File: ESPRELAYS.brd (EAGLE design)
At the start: 47 x 78 mm, 67 parts, among them IC1 ESP12SMT, J1 2.1MM DC Jack, K1 REED, K2 REED, K3 REED, K4 REED, K5 REED, K6 REED, Q1 2N7002, Q2 2N7002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

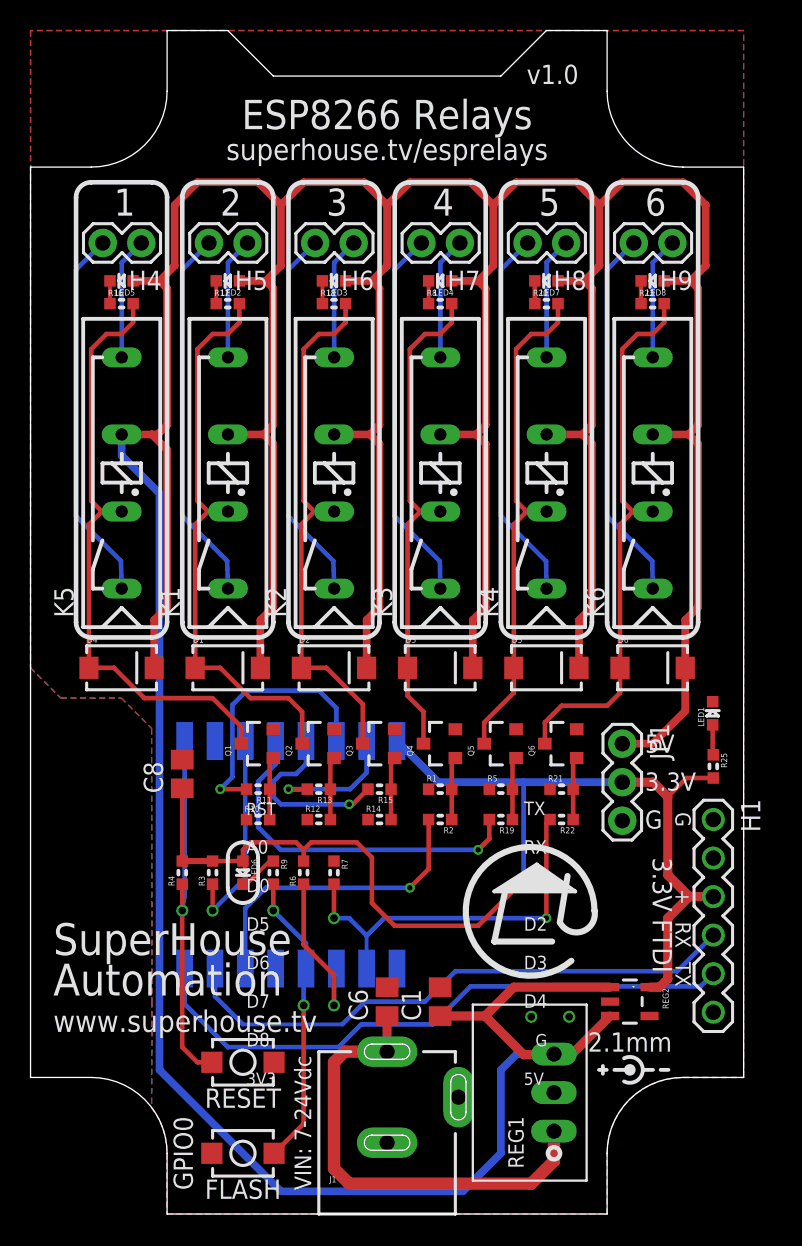
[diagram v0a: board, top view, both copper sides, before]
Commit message: Changed output pins to avoid GPIO16 because it pulses on startup. v1.1 release
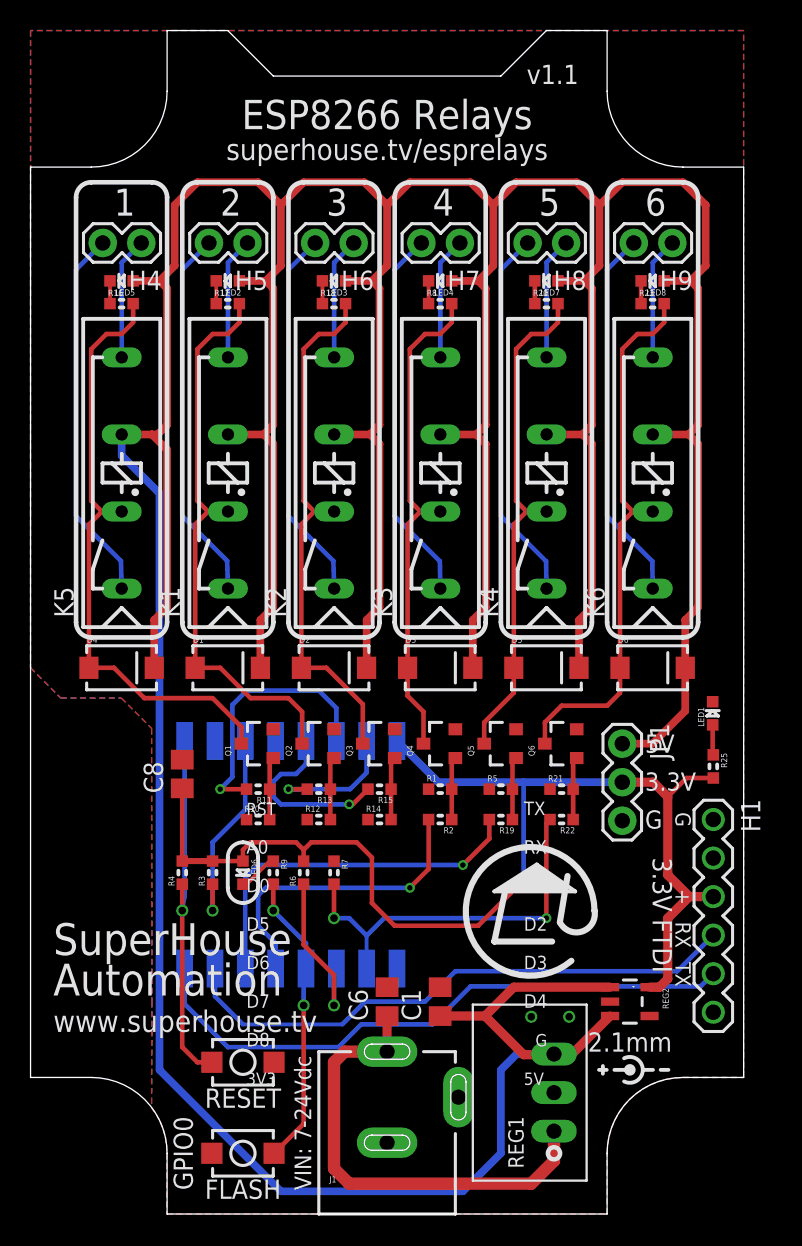
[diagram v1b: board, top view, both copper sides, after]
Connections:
- net GPIO16: no longer R19.2
- net GPIO4: now also R2.2
- net GPIO5: now also R19.2; no longer R2.2
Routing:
- net GPIO16: track 23.6 -> 0.00 mm, vias 1 -> 0
- net GPIO4: track 0.00 -> 20.5 mm, vias 0 -> 1
- net GPIO5: track 20.4 -> 24.4 mm
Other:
- board text added: "Output 1: GPIO12 Output 2: GPIO13 Output 3: GPIO14 Output 4: GPIO4 Output 5: GPIO5 Output 6: GPIO15"
- board text added: "v1.1"
- board text removed: "Output 1: GPIO12 Output 2: GPIO13 Output 3: GPIO14 Output 4: GPIO5 Output 5: GPIO16 Output 6: GPIO15"
- board text removed: "v1.0"
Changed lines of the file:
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@@
 <layer number="14" name="Route14" color="1" fill="6" visible="no" active="no"/>
 <layer number="15" name="Route15" color="4" fill="6" visible="no" active="no"/>
-<layer number="16" name="Bottom" color="1" fill="1" visible="no" active="yes"/>
+<layer number="16" name="Bottom" color="1" fill="1" visible="yes" active="yes"/>
 <layer number="17" name="Pads" color="2" fill="1" visible="yes" active="yes"/>
 <layer number="18" name="Vias" color="2" fill="1" visible="yes" active="yes"/>
 <layer number="19" name="Unrouted" color="12" fill="1" visible="yes" active="yes"/>
 <layer number="20" name="Dimension" color="15" fill="1" visible="yes" active="yes"/>
-<layer number="21" name="tPlace" color="15" fill="1" visible="no" active="yes"/>
-<layer number="22" name="bPlace" color="14" fill="1" visible="no" active="yes"/>
+<layer number="21" name="tPlace" color="15" fill="1" visible="yes" active="yes"/>
+<layer number="22" name="bPlace" color="14" fill="1" visible="yes" active="yes"/>
 <layer number="23" name="tOrigins" color="15" fill="1" visible="yes" active="yes"/>
 <layer number="24" name="bOrigins" color="3" fill="1" visible="yes" active="yes"/>
 <layer number="25" name="tNames" color="7" fill="1" visible="no" active="yes"/>
 <layer number="26" name="bNames" color="3" fill="1" visible="no" active="yes"/>
-<layer number="27" name="tValues" color="7" fill="1" visible="yes" active="yes"/>
+<layer number="27" name="tValues" color="7" fill="1" visible="no" active="yes"/>
 <layer number="28" name="bValues" color="3" fill="1" visible="no" active="yes"/>
 <layer number="29" name="tStop" color="7" fill="3" visible="no" active="yes"/>
@@
 <wire x1="32.854" y1="22.022" x2="33.362" y2="22.276" width="0.4064" layer="21"/>
 <text x="23.5" y="69.4632" size="1.4" layer="21" font="vector" ratio="15" rot="SR0" align="bottom-center">superhouse.tv/esprelays</text>
-<text x="32.698" y="74.476" size="1.27" layer="21" font="vector" ratio="18">v1.0</text>
+<text x="32.698" y="74.476" size="1.27" layer="21" font="vector" ratio="18">v1.1</text>
 <text x="31.16" y="72.476" size="1.27" layer="22" font="vector" ratio="18" rot="MR0">SKU: ESPRELAYS</text>
 <text x="18.5" y="6" size="1.1" layer="21" font="vector" ratio="18" rot="SR90" align="bottom-center">VIN: 7-24Vdc</text>
@@
 Output 2: GPIO13
 Output 3: GPIO14
-Output 4: GPIO5
-Output 5: GPIO16
+Output 4: GPIO4
+Output 5: GPIO5
 Output 6: GPIO15</text>
 <wire x1="39.119" y1="10.262" x2="39.119" y2="8.738" width="0.254" layer="21" curve="-233.130102"/>
@@
 <signal name="GPIO5">
 <contactref element="IC1" pad="14"/>
+<wire x1="14.154" y1="22.154" x2="14.154" y2="16.178" width="0.3048" layer="16"/>
+<wire x1="14.154" y1="22.154" x2="15" y2="23" width="0.3048" layer="16"/>
+<via x="28.5" y="23" extent="1-16" drill="0.3556"/>
+<wire x1="28.5" y1="23" x2="15" y2="23" width="0.3048" layer="16"/>
+<wire x1="28.5" y1="23" x2="30.238" y2="24.738" width="0.3048" layer="1"/>
+<contactref element="R19" pad="2"/>
+<wire x1="30.238" y1="24.738" x2="30.238" y2="26" width="0.3048" layer="1"/>
+</signal>
+<signal name="GPIO4">
+<contactref element="IC1" pad="13"/>
 <contactref element="R2" pad="2"/>
-<wire x1="14.154" y1="20.154" x2="14.154" y2="16.178" width="0.3048" layer="16"/>
-<wire x1="14.154" y1="20.154" x2="15.5" y2="21.5" width="0.3048" layer="16"/>
+<wire x1="16.154" y1="16.178" x2="16.154" y2="17.846" width="0.3048" layer="16"/>
+<wire x1="15" y1="19" x2="15" y2="21" width="0.3048" layer="16"/>
+<wire x1="15" y1="21" x2="15.5" y2="21.5" width="0.3048" layer="16"/>
+<wire x1="15.5" y1="21.5" x2="25" y2="21.5" width="0.3048" layer="16"/>
 <via x="25" y="21.5" extent="1-16" drill="0.3556"/>
-<wire x1="15.5" y1="21.5" x2="25" y2="21.5" width="0.3048" layer="16"/>
 <wire x1="25" y1="21.5" x2="26.238" y2="22.738" width="0.3048" layer="1"/>
 <wire x1="26.238" y1="22.738" x2="26.238" y2="26" width="0.3048" layer="1"/>
-</signal>
-<signal name="GPIO4">
-<contactref element="IC1" pad="13"/>
+<wire x1="16.154" y1="17.846" x2="15" y2="19" width="0.3048" layer="16"/>
 </signal>
 <signal name="GPIO14">
@@
 <signal name="GPIO16">
 <contactref element="IC1" pad="4"/>
-<contactref element="R19" pad="2"/>
-<wire x1="30.238" y1="26" x2="30.238" y2="24.738" width="0.3048" layer="1"/>
-<wire x1="30.238" y1="24.738" x2="29.5" y2="24" width="0.3048" layer="1"/>
-<via x="29.5" y="24" extent="1-16" drill="0.3556"/>
-<wire x1="16.5" y1="24" x2="15" y2="25.5" width="0.3048" layer="16"/>
-<wire x1="15" y1="25.5" x2="15" y2="28.5" width="0.3048" layer="16"/>
-<wire x1="16.154" y1="29.654" x2="16.154" y2="31.178" width="0.3048" layer="16"/>
-<wire x1="29.5" y1="24" x2="16.5" y2="24" width="0.3048" layer="16"/>
-<wire x1="15" y1="28.5" x2="16.154" y2="29.654" width="0.3048" layer="16"/>
 </signal>
 <signal name="GPIO0">
@@
 <wire x1="12" y1="21.738" x2="12" y2="20" width="0.3048" layer="1"/>
 <via x="12" y="20" extent="1-16" drill="0.5"/>
-<wire x1="12" y1="20" x2="14.154" y2="22.154" width="0.3048" layer="16"/>
-<wire x1="14.154" y1="22.154" x2="14.154" y2="31.178" width="0.3048" layer="16"/>
+<wire x1="14.154" y1="26.654" x2="12" y2="24.5" width="0.3048" layer="16"/>
+<wire x1="12" y1="20" x2="12" y2="24.5" width="0.3048" layer="16"/>
+<wire x1="14.154" y1="26.654" x2="14.154" y2="31.178" width="0.3048" layer="16"/>
 </signal>
 <signal name="ADC">

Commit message: Replaced most parts using SuperHouse library to add 3D models
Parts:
- removed H1: USB-TTL, freetronics:1X06
- added J2: Program, SuperHouse-Connectors:1X06-S
- C1, C6, C8: device freetronics-jon:C0805 -> SuperHouse-DiscreteSemi:C0805
- D1, D2, D3, D4, D5, D6: device SparkFun:SMA-DIODE -> SuperHouse-DiscreteSemi:SMA-DIODE
- H4, H5, H6, H7, H8, H9: device freetronics-jon:1X02 -> SuperHouse-Connectors:1X02-P
- IC1: value ESP12SMT -> ESP12-SMT; device freetronics-jon:ESP12 -> SuperHouse-MCUs:ESP12
- J1: device freetronics-jon:POWER_JACK_PTH_SLOTS -> SuperHouse-Connectors:POWER_JACK_SLOTS
- JP1: device freetronics-jon:1X03 -> SuperHouse-Connectors:1X03
- K1, K2, K3, K4, K5, K6: value REED -> REED-SIL; device relay:REED -> SuperHouse-Relays:REED
- LED1: device freetronics-jon:LED-0603 -> SuperHouse-LEDs:LED-0603
- LED2, LED3, LED4, LED5, LED6, LED7, LED8: device freetronics-master-v1:LED-0603 -> SuperHouse-LEDs:LED-0603
- Q1, Q2, Q3, Q4, Q5, Q6: device freetronics-master-v1:SOT23-3 -> SuperHouse-DiscreteSemi:SOT23-3
- R1, R10, R11, R12, R13, R14, R15, R16, R17, R18, R19, R2, R20, R21, R22, R23, R5, R8, R9: device freetronics-master-v1:0603 -> SuperHouse-DiscreteSemi:R0603
- R25, R3, R4, R6, R7: device freetronics-jon:0603 -> SuperHouse-DiscreteSemi:R0603
- REG1: device freetronics-jon:K78XX-500R3 -> SuperHouse-Regulators:K78XX-500R3
- REG2: device freetronics-jon:SOT23-5 -> SuperHouse-Regulators:SOT23-5
- S1, S2: device freetronics-jon:TACTILE_SWITCH_SMD_2PIN_TINY -> SuperHouse-Switches:TACTILE_SMD_3X4X2
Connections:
- net 3.3V: now also J2.6; no longer H1.3
- net GND: now also J2.3; no longer H1.1
- net GPIO0: now also J2.1
- net RST: now also J2.2
- net RX: now also J2.5; no longer H1.4
- net TX: now also J2.4; no longer H1.5
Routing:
- net RST: track 24.3 -> 73.6 mm, vias 1 -> 3
- net GPIO0: track 19.5 -> 50.9 mm
- net 3.3V: track 80.2 -> 81.4 mm
- net TX: track 40.4 -> 41.4 mm, vias 0 -> 1
- net GPIO15: track 26.0 -> 26.5 mm
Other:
- board text added: "ESProg"
- board text added: "GND"
- board text added: "IO0"
- board text added: "RXi"
- board text added: "TXo"
- board text added: "v1.2"
- board text removed: "+"
- board text removed: "3.3V FTDI"
- board text removed: "v1.1"
